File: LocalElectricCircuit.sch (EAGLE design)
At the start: 43 parts, among them IC1 PIC32MX360F512L, J1 Prog. Port, J3 Prog. Port, T1 PN100, U1 ADS1118, U2 ADS1118

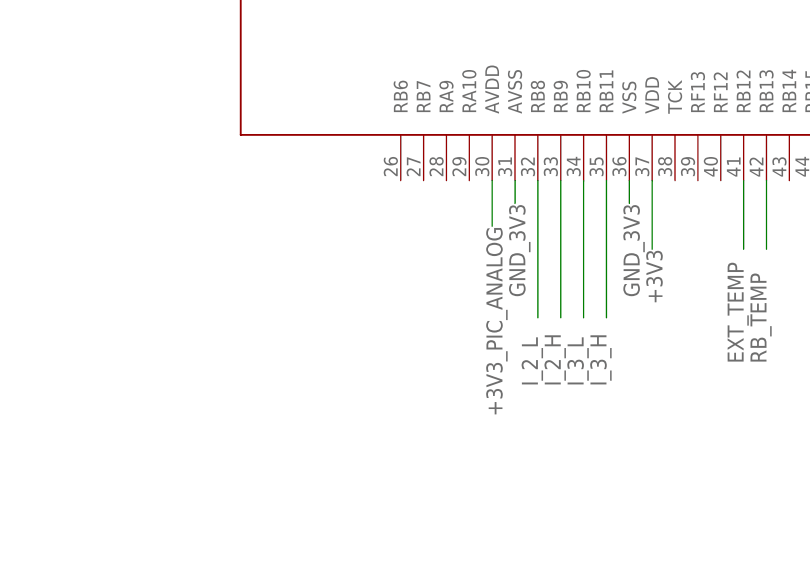
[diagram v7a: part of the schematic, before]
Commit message: THIS HERE PIC32 COULD JUST NOT LEARN ANYTHING NEW UNTIL NETS RENAMED WERE TWO
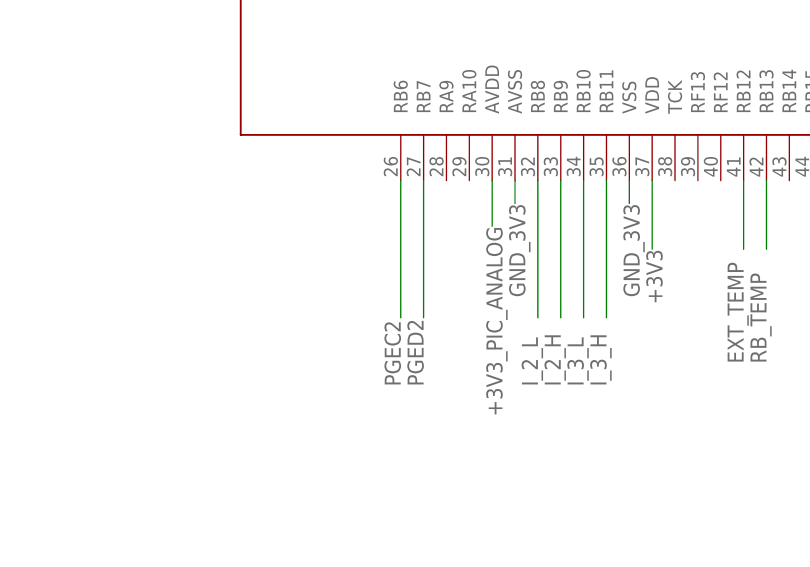
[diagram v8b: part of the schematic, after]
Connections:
- net PGEC2: now also IC1.RB6
- net PGED2: now also IC1.RB7
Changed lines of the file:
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@@
 <label x="15.24" y="127.635" size="1.778" layer="95" rot="R180"/>
+</segment>
+<segment>
+<pinref part="IC1" gate="G$1" pin="RB6"/>
+<wire x1="40.64" y1="7.62" x2="40.64" y2="-7.62" width="0.1524" layer="91"/>
+<label x="40.64" y="-15.24" size="1.778" layer="95" rot="R90"/>
 </segment>
 </net>
@@
 <label x="15.24" y="130.175" size="1.778" layer="95" rot="R180"/>
 </segment>
+<segment>
+<pinref part="IC1" gate="G$1" pin="RB7"/>
+<wire x1="43.18" y1="7.62" x2="43.18" y2="-7.62" width="0.1524" layer="91"/>
+<label x="43.18" y="-15.24" size="1.778" layer="95" rot="R90"/>
+</segment>
 </net>
